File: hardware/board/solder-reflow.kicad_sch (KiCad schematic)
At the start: 51 parts, among them J1 AC_Con, J2 OLED 0.91, J3 PTC_Con, J4 Barrel_Jack_Switch_Pin3Ring, K1 G3MB202PDC12, Q1 BC557, SW1 RotaryEncoder_Switch, U1 TL431LP, U2 OPA2134, U3 OPA2134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

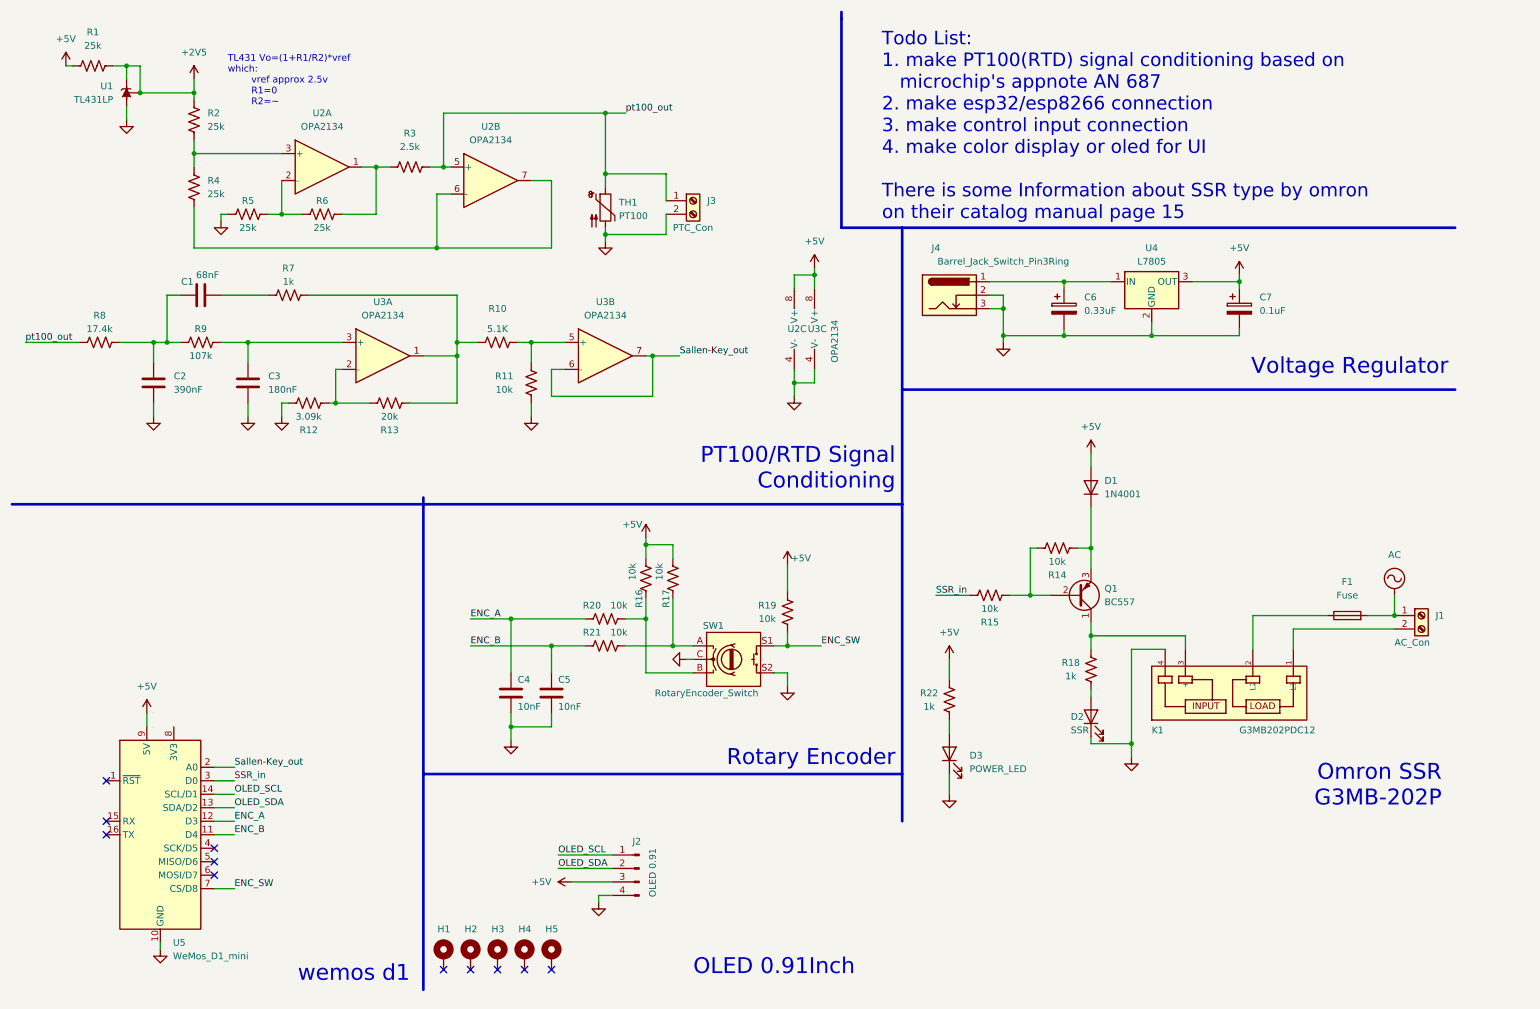
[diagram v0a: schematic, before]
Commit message: route rotated wemos and make order to jlc pcb
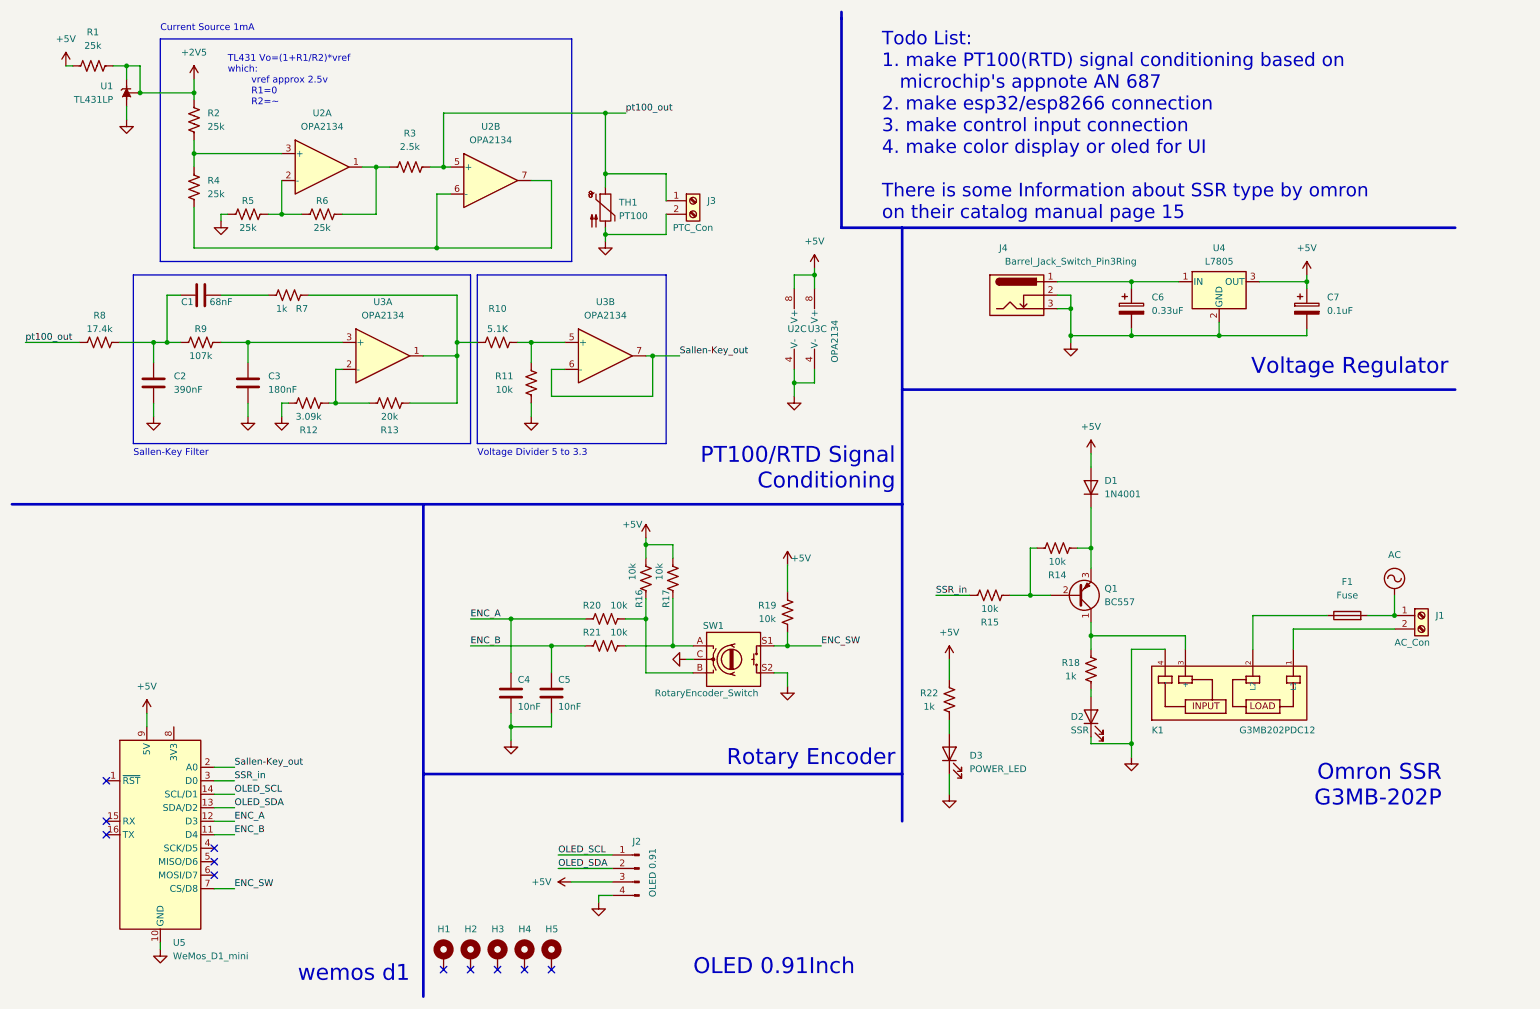
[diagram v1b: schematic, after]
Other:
- note added: "Current Source 1mA"
- note added: "Sallen-Key Filter"
- note added: "Voltage Divider 5 to 3.3"
- moved on the sheet: C6, C7, J4, U4
